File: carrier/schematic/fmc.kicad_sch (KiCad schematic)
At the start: 12 parts, among them J801 ASP-134603-01, U801 TLV75725PDBVR

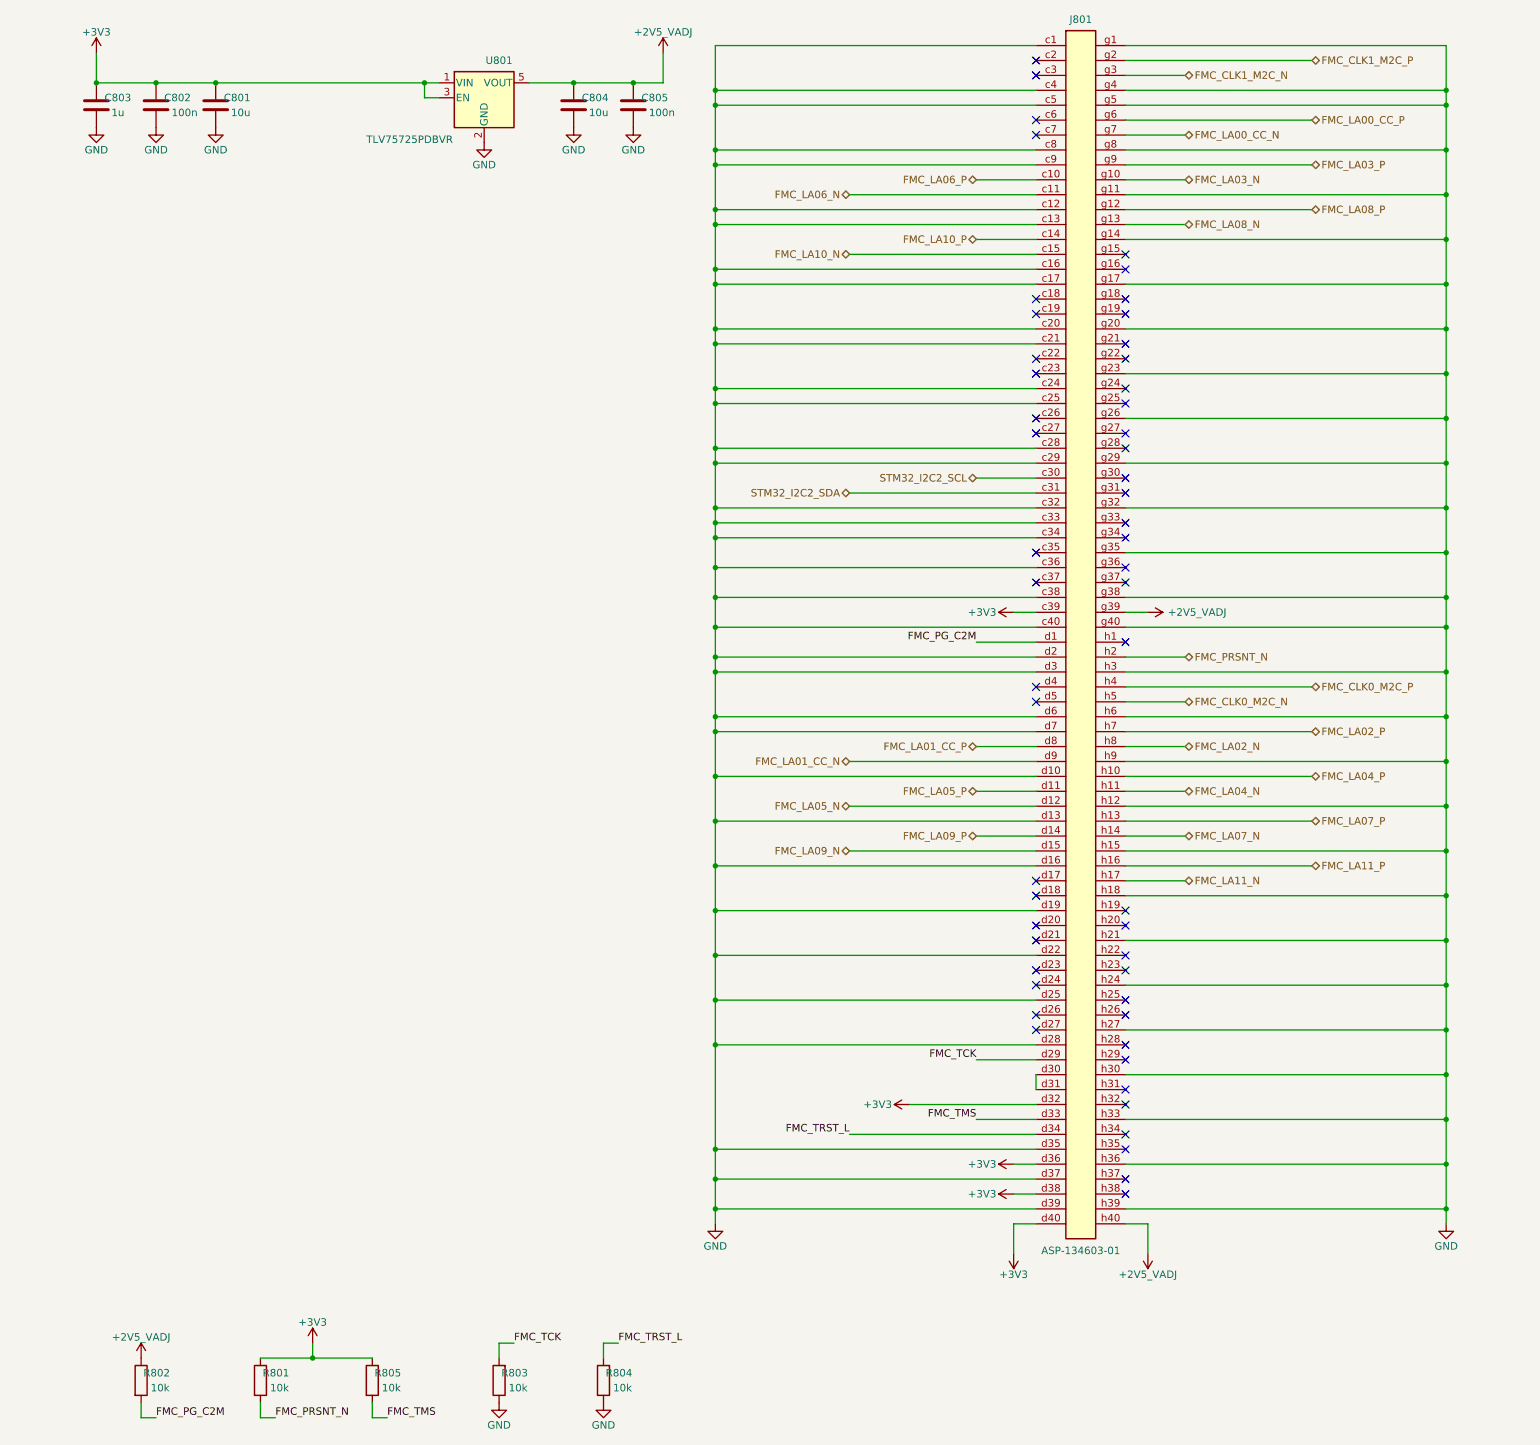
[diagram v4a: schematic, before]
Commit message: testpoints: TEST-POINT COVERAGE GATE (round 4) — engine probe rows + 42 TPs
- model.py API (landed with U1): c.testpoint(net) = Connector:TestPoint on
  TestPoint:TestPoint_Pad_D1.5mm, BOM=exclude (copper only — BOM/preflight
  exporters skip it; bom_jlc.csv stays 76 lines); c.waive_tp(net, reason).
- schgen/testpoints.py + place.build hook: TPs are STRIPPED before the
  topology templates run (a probe point can never perturb the circuit's
  layout), then the ENGINE appends a dedicated probe row below the extent:
  GND cells (TP + ground symbol), rail cells (rail glyph + stub + TP, name
  shown once as the TP Value), PORT cells (labeled islet — route.py's
  every-islet-labeled rule, netlist gate proves the merge). Rows wrap
  cell-width-aware and cap at extent-center+20mm so they can never reach
  the frame's title block; sheets riding the A3 height budget (fmc) get a
  vertical probe column right of the fan instead.
- COVERAGE GATE in schgen board: every POWER/GROUND rail + key bus (i2c
  ports, sd_bus CMD/CLK, UART RXD/TXD, EN lines per the bring-up
  philosophy) owns a TP or an explicit waiver; report with verbatim
  waivers: carrier/reports/testpoints.txt — PASS 43/52 covered, 9 waived
  (4x power_mon shunt stubs pending the rail split, 4x VCCO awaiting the
  wave-3 rail-map regen, CHASSIS_GND probeable at every shell tab).
- 42 TPs authored at their owning sheets (rails at their source: power,
  bringup_modules switch outputs, fmc VADJ, pd_input +VIN inlet; buses:
  STM32_I2C2/CAM/CTP/DDC, SDIO CMD/CLK 1.8V side, UART0, all 13 EN lines
  + CAM_EN + VBUS_OUT_EN).
- RENDERS: all 12 drifted sheets inspected by eye at full resolution and
  hand-drawn-clean before blessing:
  power (4-cell row, clean), bringup_en (3 EN cells), bringup_en_modules
  (9 cells wrapped 5+4, clear of title block — first attempt overlapped
  it, fixed via the wrap), bringup_modules (8 rail cells wrapped 7+1),
  bringup_rails (SC rail + I2C pair), camera (I2C + EN), fmc (vertical
  VADJ cel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
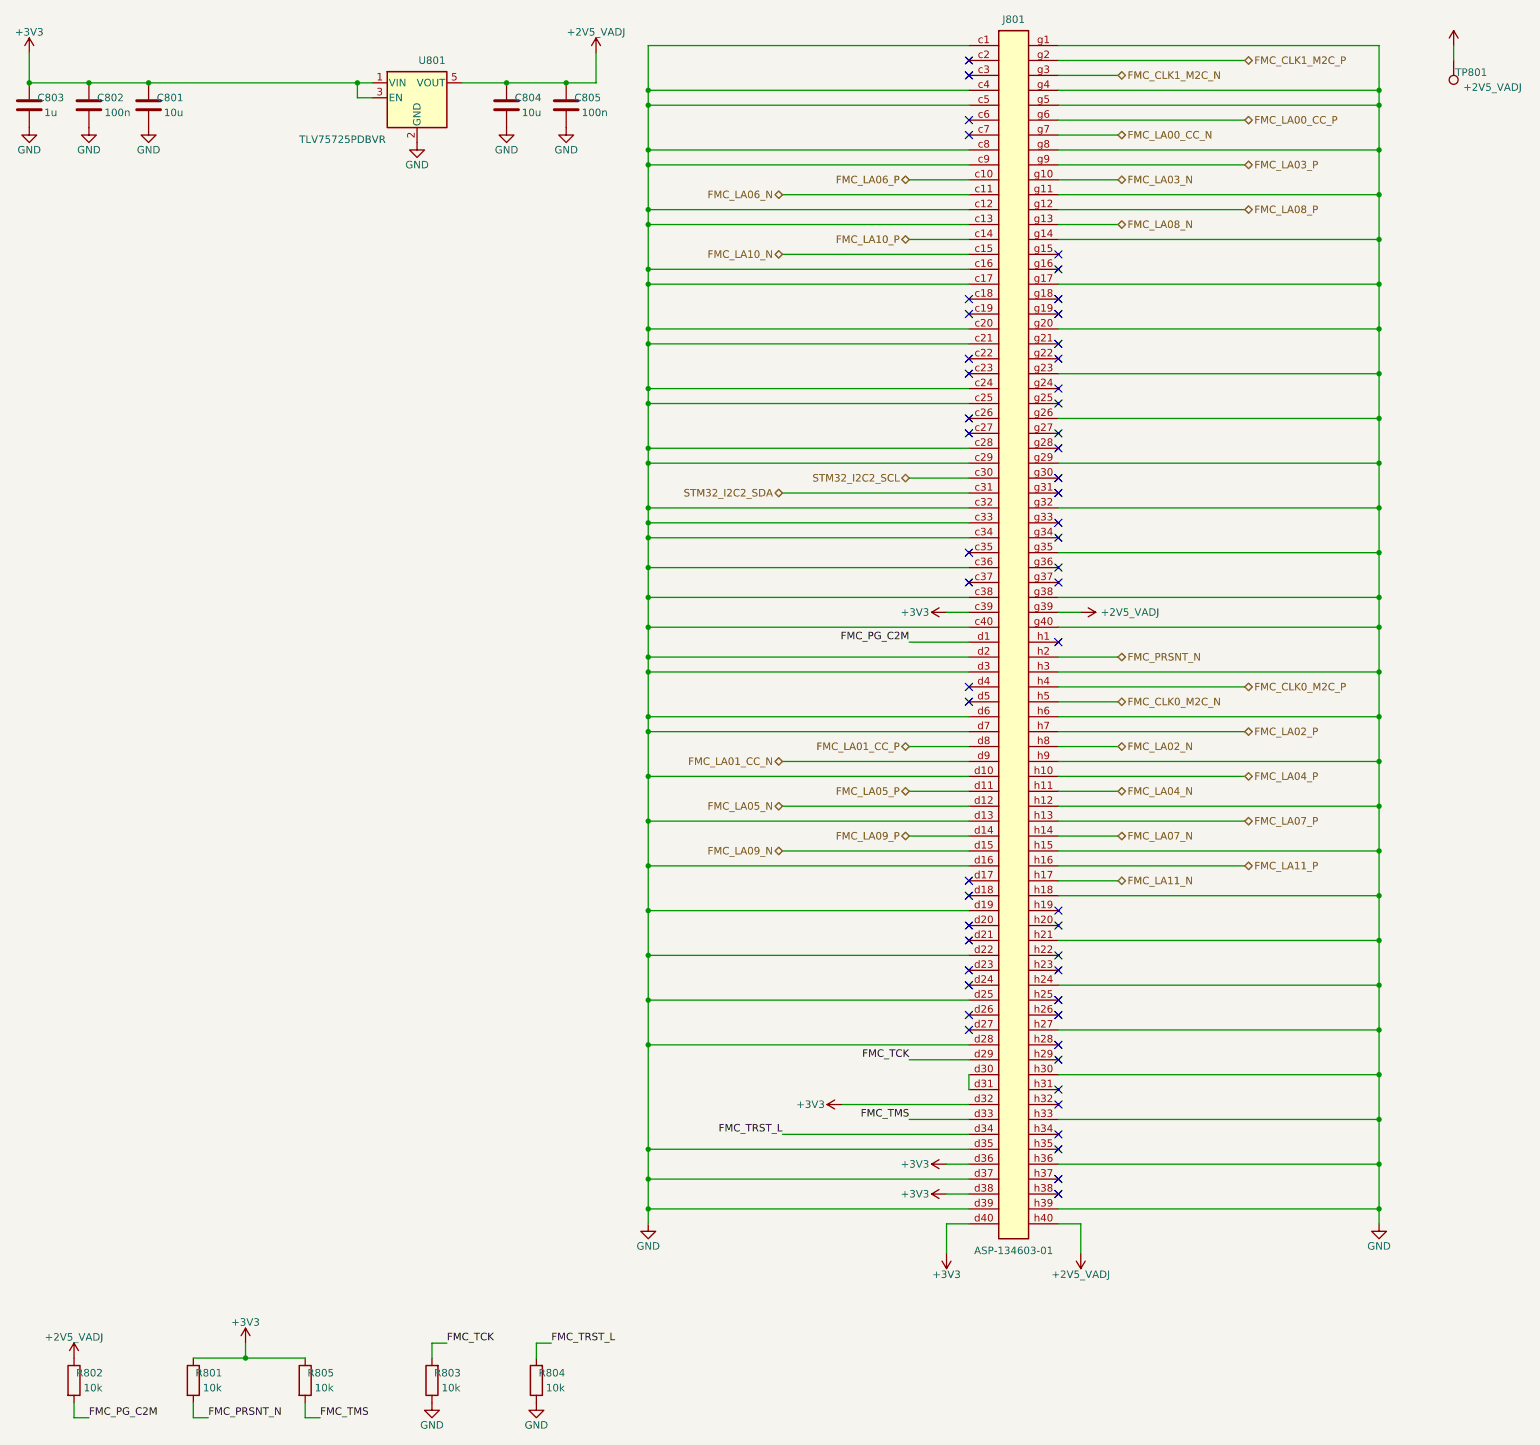
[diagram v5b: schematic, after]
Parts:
- added TP801: +2V5_VADJ, TestPoint:TestPoint_Pad_D1.5mm, symbol Connector:TestPoint
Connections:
- net +2V5_VADJ: now also TP801.1

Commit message: audit-fix(engine): harvest F1-F7,F9 — gate hardening + leak + guards
F1 selftest now exercises the VISUAL gate against geometry mutants (wire-cross
+ text-over-wire) — proven to bite (was never run on a mutant before).
F2 visual_gate catches different-net wire T-touch / butt-join shorts.
F3 netlist_gate no longer leaks tmp .net files (was 2671 stale).
F4 board uniquify guards the stride (widened 100->1000) against ref collision.
F5 hier-mode sheets now re-run through the per-sheet netlist gate.
F6 dead clause dropped; F7 stale zynq_eda docstring fixed; F9 eager inline-pin
validation. Source copied verbatim from the audit-fix worktree (6 files, proven
untouched on origin since its base); board regenerated fresh. All gates green,
selftest geo-mutants killed by the visual gate, goldens 23/23, m1_rc PASS.

Co-Authored-By: Claude Fable 5 <noreply@anthropic.com>
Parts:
- renumbered C801 to C8001, C802 to C8002, C803 to C8003, C804 to C8004, C805 to C8005, J801 to J8001, R801 to R8001, R802 to R8002, R803 to R8003, R804 to R8004, R805 to R8005, TP801 to TP8001, U801 to U8001
